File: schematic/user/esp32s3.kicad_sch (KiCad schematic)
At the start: 12 parts, among them J4 I2C Breakout, SW1 ESP32S3 Reset, SW2 ESP32S3 Boot Method, U5 ESP32-S3-WROOM-1-N16R8

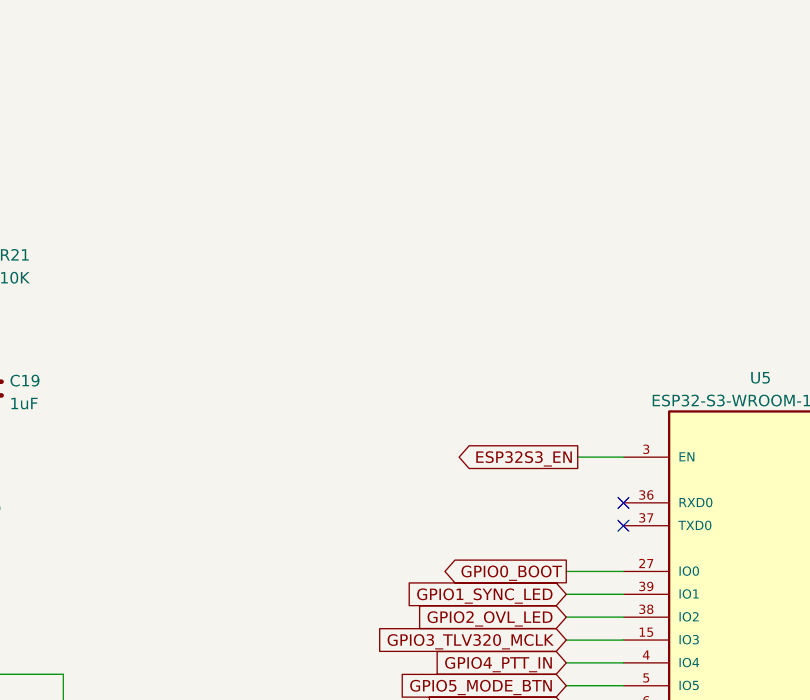
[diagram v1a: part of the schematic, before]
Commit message: v0.6 board: add UART0 header to assist with ESP RF Test Tool.
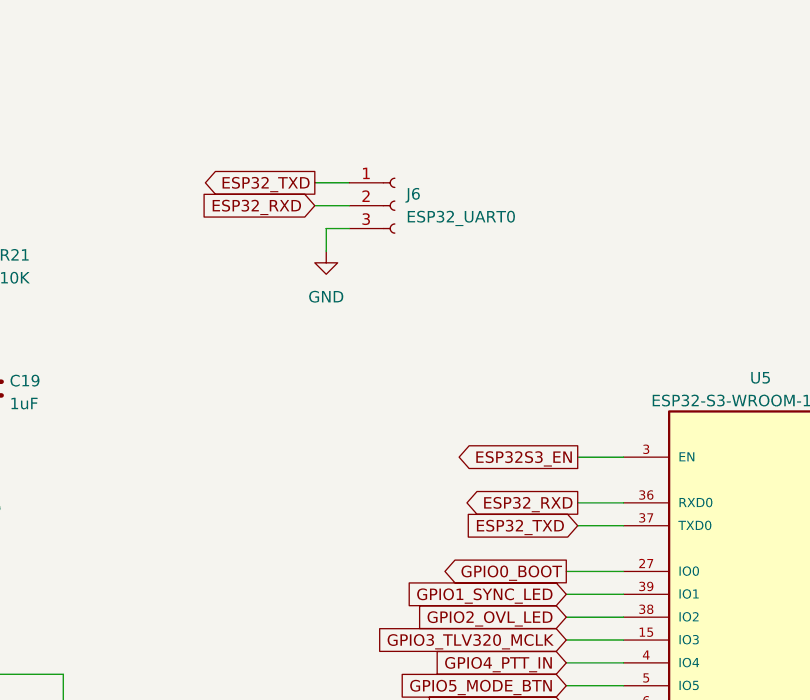
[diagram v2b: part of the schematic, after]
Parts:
- added J6: ESP32_UART0, Connector_PinHeader_2.54mm:PinHeader_1x03_P2.54mm_Vertical, symbol Connector:Conn_01x03_Female
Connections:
- net GND: now also J6.3 (Pin_3)
- net ESP32_RXD: now reaches U5.36 (RXD0)
- net ESP32_RXD: now also J6.2 (Pin_2)
- net ESP32_TXD: now reaches U5.37 (TXD0)
- net ESP32_TXD: now also J6.1 (Pin_1)
- no-connect marks 10 -> 8
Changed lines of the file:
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@@
   (no_connect (at 187.96 107.95))
   (no_connect (at 187.96 105.41))
-  (no_connect (at 157.48 77.47))
-  (no_connect (at 157.48 80.01))
   (no_connect (at 187.96 110.49))
   (no_connect (at 187.96 113.03))
@@
     (stroke (width 0) (type default) (color 0 0 0 0))
   )
+  (wire (pts (xy 123.19 44.45) (xy 127 44.45))
+    (stroke (width 0) (type default) (color 0 0 0 0))
+  )
   (wire (pts (xy 124.46 163.83) (xy 124.46 165.1))
     (stroke (width 0) (type default) (color 0 0 0 0))
@@
     (stroke (width 0) (type default) (color 0 0 0 0))
   )
+  (wire (pts (xy 152.4 80.01) (xy 157.48 80.01))
+    (stroke (width 0) (type default) (color 0 0 0 0))
+  )
   (wire (pts (xy 63.5 149.86) (xy 71.12 149.86))
     (stroke (width 0) (type default) (color 0 0 0 0))
@@
     (stroke (width 0) (type default) (color 0 0 0 0))
   )
+  (wire (pts (xy 152.4 77.47) (xy 157.48 77.47))
+    (stroke (width 0) (type default) (color 0 0 0 0))
+  )
   (wire (pts (xy 187.96 123.19) (xy 194.31 123.19))
     (stroke (width 0) (type default) (color 0 0 0 0))
@@
     (stroke (width 0) (type default) (color 0 0 0 0))
   )
+  (wire (pts (xy 123.19 41.91) (xy 127 41.91))
+    (stroke (width 0) (type default) (color 0 0 0 0))
+  )
   (wire (pts (xy 152.4 72.39) (xy 157.48 72.39))
     (stroke (width 0) (type default) (color 0 0 0 0))
@@
     (stroke (width 0) (type default) (color 0 0 0 0))
   )
+  (wire (pts (xy 124.46 46.99) (xy 124.46 49.53))
+    (stroke (width 0) (type default) (color 0 0 0 0))
+  )
   (wire (pts (xy 86.36 41.91) (xy 86.36 46.99))
     (stroke (width 0) (type default) (color 0 0 0 0))
@@
     (stroke (width 0) (type default) (color 0 0 0 0))
   )
+  (wire (pts (xy 127 46.99) (xy 124.46 46.99))
+    (stroke (width 0) (type default) (color 0 0 0 0))
+  )
   (wire (pts (xy 71.12 149.86) (xy 71.12 156.21))
     (stroke (width 0) (type default) (color 0 0 0 0))
@@
     )
   )
+  (global_label "ESP32_TXD" (shape output) (at 123.19 41.91 180) (fields_autoplaced)
+    (effects (font (size 1.27 1.27)) (justify right))
+    (property "Intersheet References" "${INTERSHEET_REFS}" (id 0) (at 110.3145 41.8306 0)
+      (effects (font (size 1.27 1.27)) (justify right) hide)
+    )
+  )
   (global_label "3.3V" (shape output) (at 86.36 41.91 90) (fields_autoplaced)
     (effects (font (size 1.27 1.27)) (justify left))
@@
     )
   )
+  (global_label "ESP32_TXD" (shape input) (at 152.4 80.01 180) (fields_autoplaced)
+    (effects (font (size 1.27 1.27)) (justify right))
+    (property "Intersheet References" "${INTERSHEET_REFS}" (id 0) (at 139.5245 79.9306 0)
+      (effects (font (size 1.27 1.27)) (justify right) hide)
+    )
+  )
+  (global_label "ESP32_RXD" (shape input) (at 123.19 44.45 180) (fields_autoplaced)
+    (effects (font (size 1.27 1.27)) (justify right))
+    (property "Intersheet References" "${INTERSHEET_REFS}" (id 0) (at 110.0121 44.3706 0)
+      (effects (font (size 1.27 1.27)) (justify right) hide)
+    )
+  )
   (global_label "ESP32S3_EN" (shape input) (at 67.31 96.52 180) (fields_autoplaced)
     (effects (font (size 1.27 1.27)) (justify right))
@@
     (property "Intersheet References" "${INTERSHEET_REFS}" (id 0) (at 216.6198 87.5506 0)
       (effects (font (size 1.27 1.27)) (justify left) hide)
+    )
+  )
+  (global_label "ESP32_RXD" (shape output) (at 152.4 77.47 180) (fields_autoplaced)
+    (effects (font (size 1.27 1.27)) (justify right))
+    (property "Intersheet References" "${INTERSHEET_REFS}" (id 0) (at 139.2221 77.5494 0)
+      (effects (font (size 1.27 1.27)) (justify right) hide)
     )
   )
@@
     (pin "2")
   )
+  (symbol (lib_id "power:GND") (at 124.46 49.53 0) (unit 1)
+    (in_bom yes) (on_board yes) (fields_autoplaced)
+    (property "Reference" "#PWR044" (id 0) (at 124.46 55.88 0)
+      (effects (font (size 1.27 1.27)) hide)
+    )
+    (property "Value" "GND" (id 1) (at 124.46 54.61 0))
+    (property "Footprint" "" (id 2) (at 124.46 49.53 0)
+      (effects (font (size 1.27 1.27)) hide)
+    )
+    (property "Datasheet" "" (id 3) (at 124.46 49.53 0)
+      (effects (font (size 1.27 1.27)) hide)
+    )
+    (pin "1")
+  )
   (symbol (lib_id "power:GND") (at 207.01 44.45 0) (unit 1)
     (in_bom yes) (on_board yes) (fields_autoplaced)
@@
     (pin "1")
   )
+  (symbol (lib_id "Connector:Conn_01x03_Female") (at 132.08 44.45 0) (unit 1)
+    (in_bom yes) (on_board yes) (fields_autoplaced)
+    (property "Reference" "J6" (id 0) (at 133.35 43.1799 0)
+      (effects (font (size 1.27 1.27)) (justify left))
+    )
+    (property "Value" "ESP32_UART0" (id 1) (at 133.35 45.7199 0)
+      (effects (font (size 1.27 1.27)) (justify left))
+    )
+    (property "Footprint" "Connector_PinHeader_2.54mm:PinHeader_1x03_P2.54mm_Vertical" (id 2) (at 132.08 44.45 0)
+      (effects (font (size 1.27 1.27)) hide)
+    )
+    (property "Datasheet" "~" (id 3) (at 132.08 44.45 0)
+      (effects (font (size 1.27 1.27)) hide)
+    )
+    (pin "1")
+    (pin "2")
+    (pin "3")
+  )
   (symbol (lib_id "power:GND") (at 86.36 73.66 0) (unit 1)

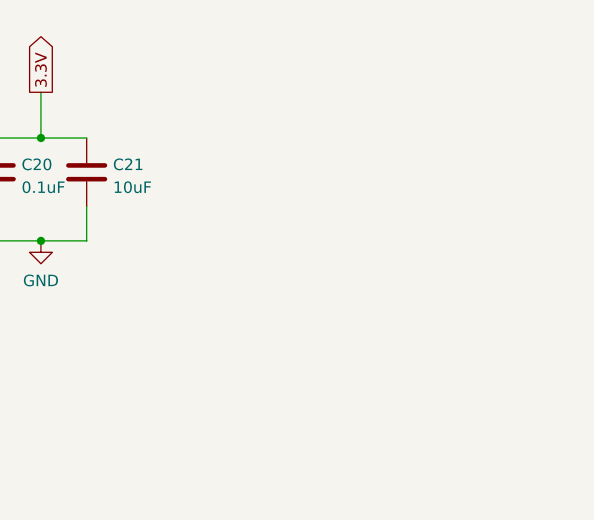
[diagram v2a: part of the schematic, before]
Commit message: v0.6 board: add J7 so that the board can be powered directly from 3.3V and GPIO/reset externally controlled.
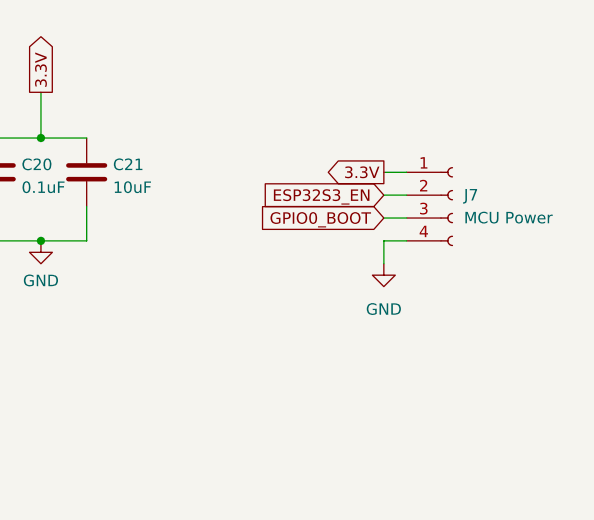
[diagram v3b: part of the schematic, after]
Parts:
- added J7: MCU Power, Connector_PinHeader_2.54mm:PinHeader_1x04_P2.54mm_Vertical, symbol Connector:Conn_01x04_Female
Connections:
- net 3.3V: now also J7.1 (Pin_1)
- net ESP32S3_EN: now also J7.2 (Pin_2)
- net GND: now also J7.4 (Pin_4)
- net GPIO0_BOOT: now also J7.3 (Pin_3)
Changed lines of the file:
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@@
+    (stroke (width 0) (type default) (color 0 0 0 0))
+  )
+  (wire (pts (xy 245.11 41.91) (xy 247.65 41.91))
     (stroke (width 0) (type default) (color 0 0 0 0))
   )
@@
     (stroke (width 0) (type default) (color 0 0 0 0))
   )
+  (wire (pts (xy 245.11 36.83) (xy 247.65 36.83))
+    (stroke (width 0) (type default) (color 0 0 0 0))
+  )
+  (wire (pts (xy 247.65 44.45) (xy 245.11 44.45))
+    (stroke (width 0) (type default) (color 0 0 0 0))
+  )
   (wire (pts (xy 151.13 107.95) (xy 157.48 107.95))
     (stroke (width 0) (type default) (color 0 0 0 0))
@@
     (stroke (width 0) (type default) (color 0 0 0 0))
   )
+  (wire (pts (xy 245.11 39.37) (xy 247.65 39.37))
+    (stroke (width 0) (type default) (color 0 0 0 0))
+  )
   (wire (pts (xy 95.25 107.95) (xy 95.25 113.03))
     (stroke (width 0) (type default) (color 0 0 0 0))
@@
     (stroke (width 0) (type default) (color 0 0 0 0))
   )
+  (wire (pts (xy 245.11 44.45) (xy 245.11 46.99))
+    (stroke (width 0) (type default) (color 0 0 0 0))
+  )
   (global_label "3.3V_PERIPH" (shape output) (at 68.58 158.75 180) (fields_autoplaced)
     (effects (font (size 1.27 1.27)) (justify right))
@@
     )
   )
+  (global_label "GPIO0_BOOT" (shape input) (at 245.11 41.91 180) (fields_autoplaced)
+    (effects (font (size 1.27 1.27)) (justify right))
+    (property "Intersheet References" "${INTERSHEET_REFS}" (id 0) (at 231.1459 41.8306 0)
+      (effects (font (size 1.27 1.27)) (justify right) hide)
+    )
+  )
   (global_label "GPIO8_BAT_ALERT" (shape output) (at 151.13 105.41 180) (fields_autoplaced)
     (effects (font (size 1.27 1.27)) (justify right))
@@
     )
   )
+  (global_label "3.3V" (shape output) (at 245.11 36.83 180) (fields_autoplaced)
+    (effects (font (size 1.27 1.27)) (justify right))
+    (property "Intersheet References" "${INTERSHEET_REFS}" (id 0) (at 238.5845 36.7506 0)
+      (effects (font (size 1.27 1.27)) (justify right) hide)
+    )
+  )
   (global_label "ESP32S3_EN" (shape input) (at 80.01 58.42 180) (fields_autoplaced)
     (effects (font (size 1.27 1.27)) (justify right))
@@
     (property "Intersheet References" "${INTERSHEET_REFS}" (id 0) (at 204.3431 92.6306 0)
       (effects (font (size 1.27 1.27)) (justify left) hide)
+    )
+  )
+  (global_label "ESP32S3_EN" (shape input) (at 245.11 39.37 180) (fields_autoplaced)
+    (effects (font (size 1.27 1.27)) (justify right))
+    (property "Intersheet References" "${INTERSHEET_REFS}" (id 0) (at 230.7831 39.4494 0)
+      (effects (font (size 1.27 1.27)) (justify right) hide)
     )
   )
@@
     (pin "4")
   )
+  (symbol (lib_id "power:GND") (at 245.11 46.99 0) (unit 1)
+    (in_bom yes) (on_board yes) (fields_autoplaced)
+    (property "Reference" "#PWR0105" (id 0) (at 245.11 53.34 0)
+      (effects (font (size 1.27 1.27)) hide)
+    )
+    (property "Value" "GND" (id 1) (at 245.11 52.07 0))
+    (property "Footprint" "" (id 2) (at 245.11 46.99 0)
+      (effects (font (size 1.27 1.27)) hide)
+    )
+    (property "Datasheet" "" (id 3) (at 245.11 46.99 0)
+      (effects (font (size 1.27 1.27)) hide)
+    )
+    (pin "1")
+  )
   (symbol (lib_id "Switch:SW_Push") (at 77.47 96.52 0) (unit 1)
     (in_bom yes) (on_board yes) (fields_autoplaced)
@@
     (pin "2")
   )
+  (symbol (lib_id "Connector:Conn_01x04_Female") (at 252.73 39.37 0) (unit 1)
+    (in_bom yes) (on_board yes) (fields_autoplaced)
+    (property "Reference" "J7" (id 0) (at 254 39.3699 0)
+      (effects (font (size 1.27 1.27)) (justify left))
+    )
+    (property "Value" "MCU Power" (id 1) (at 254 41.9099 0)
+      (effects (font (size 1.27 1.27)) (justify left))
+    )
+    (property "Footprint" "Connector_PinHeader_2.54mm:PinHeader_1x04_P2.54mm_Vertical" (id 2) (at 252.73 39.37 0)
+      (effects (font (size 1.27 1.27)) hide)
+    )
+    (property "Datasheet" "~" (id 3) (at 252.73 39.37 0)
+      (effects (font (size 1.27 1.27)) hide)
+    )
+    (pin "1")
+    (pin "2")
+    (pin "3")
+    (pin "4")
+  )
   (symbol (lib_id "Device:C") (at 212.09 36.83 0) (unit 1)

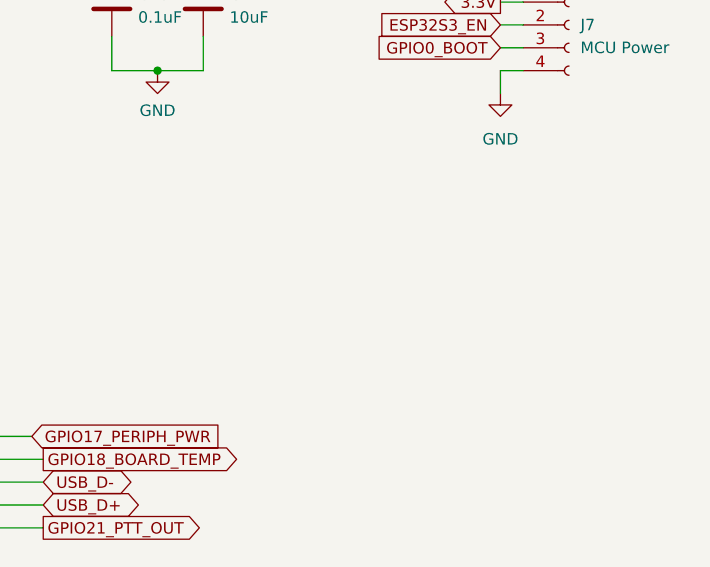
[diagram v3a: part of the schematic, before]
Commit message: v0.6 board: add output-only ULP Serial header for future ULP code debugging + regulatory use.
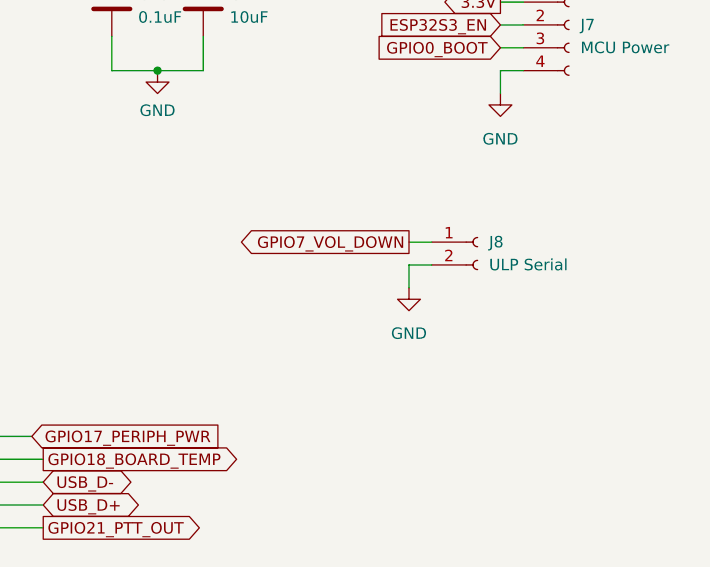
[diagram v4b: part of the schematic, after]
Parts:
- added J8: ULP Serial, Connector_PinHeader_2.54mm:PinHeader_1x02_P2.54mm_Vertical, symbol Connector:Conn_01x02_Female
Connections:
- net GND: now also J8.2 (Pin_2)
- net GPIO7_VOL_DOWN: now also J8.1 (Pin_1)
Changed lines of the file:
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@@
+    (stroke (width 0) (type default) (color 0 0 0 0))
+  )
+  (wire (pts (xy 237.49 66.04) (xy 234.95 66.04))
     (stroke (width 0) (type default) (color 0 0 0 0))
   )
@@
     (stroke (width 0) (type default) (color 0 0 0 0))
   )
+  (wire (pts (xy 234.95 63.5) (xy 237.49 63.5))
+    (stroke (width 0) (type default) (color 0 0 0 0))
+  )
   (wire (pts (xy 123.19 41.91) (xy 127 41.91))
     (stroke (width 0) (type default) (color 0 0 0 0))
@@
     (stroke (width 0) (type default) (color 0 0 0 0))
   )
+  (wire (pts (xy 234.95 66.04) (xy 234.95 68.58))
+    (stroke (width 0) (type default) (color 0 0 0 0))
+  )
   (wire (pts (xy 151.13 120.65) (xy 157.48 120.65))
     (stroke (width 0) (type default) (color 0 0 0 0))
@@
     (effects (font (size 1.27 1.27)) (justify right))
     (property "Intersheet References" "${INTERSHEET_REFS}" (id 0) (at 139.5245 79.9306 0)
+      (effects (font (size 1.27 1.27)) (justify right) hide)
+    )
+  )
+  (global_label "GPIO7_VOL_DOWN" (shape output) (at 234.95 63.5 180) (fields_autoplaced)
+    (effects (font (size 1.27 1.27)) (justify right))
+    (property "Intersheet References" "${INTERSHEET_REFS}" (id 0) (at 216.0874 63.4206 0)
       (effects (font (size 1.27 1.27)) (justify right) hide)
     )
@@
     )
     (property "LCSC" "C1525" (id 4) (at 201.93 36.83 0)
+      (effects (font (size 1.27 1.27)) hide)
+    )
+    (pin "1")
+    (pin "2")
+  )
+  (symbol (lib_id "Connector:Conn_01x02_Female") (at 242.57 63.5 0) (unit 1)
+    (in_bom yes) (on_board yes) (fields_autoplaced)
+    (property "Reference" "J8" (id 0) (at 243.84 63.4999 0)
+      (effects (font (size 1.27 1.27)) (justify left))
+    )
+    (property "Value" "ULP Serial" (id 1) (at 243.84 66.0399 0)
+      (effects (font (size 1.27 1.27)) (justify left))
+    )
+    (property "Footprint" "Connector_PinHeader_2.54mm:PinHeader_1x02_P2.54mm_Vertical" (id 2) (at 242.57 63.5 0)
+      (effects (font (size 1.27 1.27)) hide)
+    )
+    (property "Datasheet" "~" (id 3) (at 242.57 63.5 0)
       (effects (font (size 1.27 1.27)) hide)
     )
@@
     (pin "2")
   )
+  (symbol (lib_id "power:GND") (at 234.95 68.58 0) (unit 1)
+    (in_bom yes) (on_board yes) (fields_autoplaced)
+    (property "Reference" "#PWR045" (id 0) (at 234.95 74.93 0)
+      (effects (font (size 1.27 1.27)) hide)
+    )
+    (property "Value" "GND" (id 1) (at 234.95 73.66 0))
+    (property "Footprint" "" (id 2) (at 234.95 68.58 0)
+      (effects (font (size 1.27 1.27)) hide)
+    )
+    (property "Datasheet" "" (id 3) (at 234.95 68.58 0)
+      (effects (font (size 1.27 1.27)) hide)
+    )
+    (pin "1")
+  )
   (symbol (lib_id "power:GND") (at 124.46 175.26 0) (unit 1)
